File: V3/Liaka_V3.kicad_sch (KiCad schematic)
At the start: 0 parts

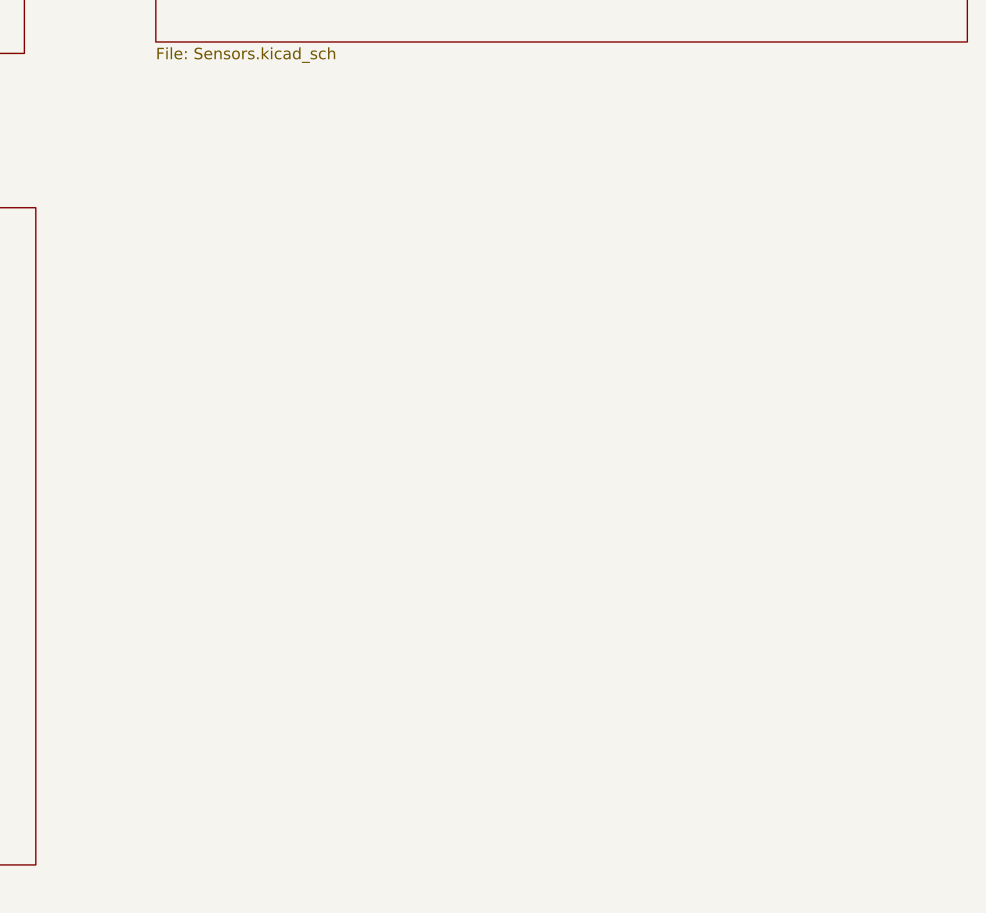
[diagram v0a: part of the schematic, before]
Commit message: Changed imu added flash chip
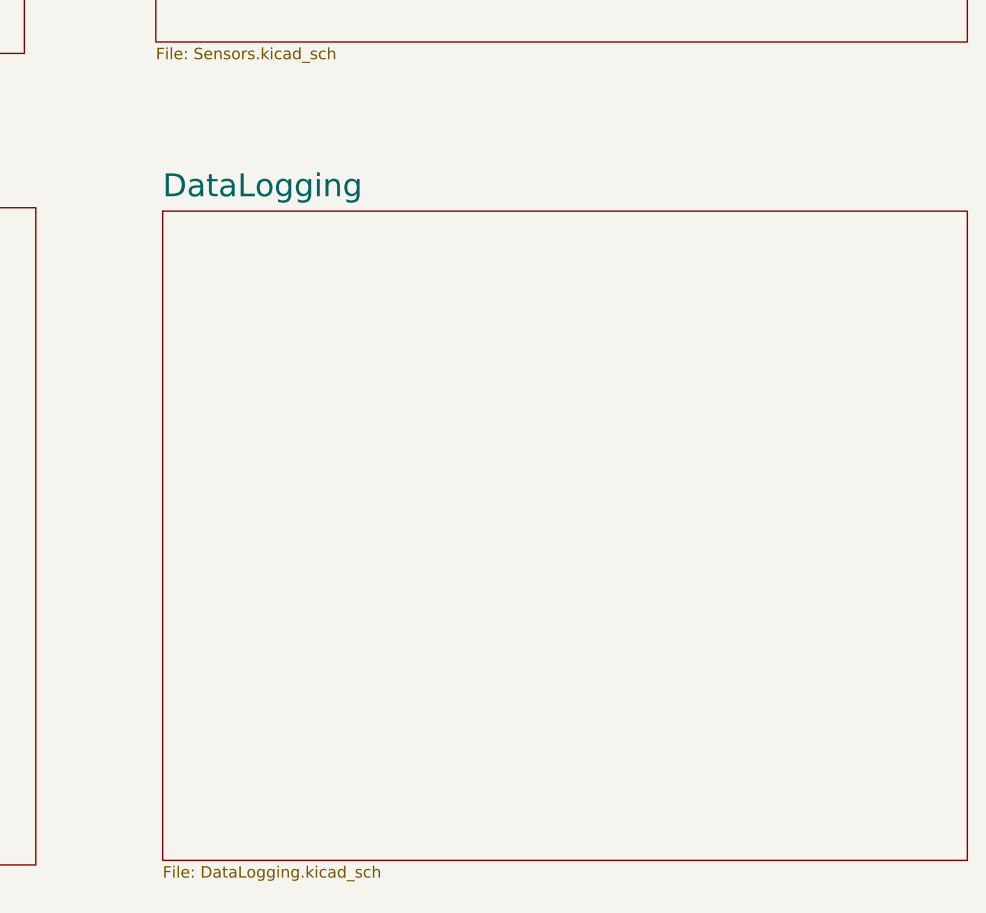
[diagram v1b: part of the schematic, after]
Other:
- added sheet DataLogging (DataLogging.kicad_sch)
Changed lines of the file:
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@@
+    )
+  )
+  (sheet (at 229.362 115.316) (size 89.408 72.136) (fields_autoplaced)
+    (stroke (width 0.1524) (type solid) (color 0 0 0 0))
+    (fill (color 8 253 255 0.2200))
+    (property "Sheet name" "DataLogging" (id 0) (at 229.362 113.9694 0)
+      (effects (font (size 2.54 2.54)) (justify left bottom))
+    )
+    (property "Sheet file" "DataLogging.kicad_sch" (id 1) (at 229.362 188.0366 0)
+      (effects (font (size 1.27 1.27)) (justify left top))
     )
   )
@@
     (path "/c1bf2b0b-bfb8-46f1-8af4-59d66c9f7f58" (page "5"))
     (path "/4e039e01-c7b4-4c31-a258-ecc90b9f543a" (page "6"))
+    (path "/38f95464-c4fd-44f7-9819-1304e1c28009" (page "7"))
   )
   (symbol_instances
@@
       (reference "#PWR?") (unit 1) (value "+BATT") (footprint "")
     )
-    (path "/4e039e01-c7b4-4c31-a258-ecc90b9f543a/07c49235-fb78-4b23-a52c-896dc2a9d0b2"
-      (reference "#PWR?") (unit 1) (value "VDD") (footprint "")
-    )
     (path "/c1bf2b0b-bfb8-46f1-8af4-59d66c9f7f58/0eab405b-23d8-4c86-88c9-b94c5ad9ac03"
       (reference "#PWR?") (unit 1) (value "VDD") (footprint "")
     )
+    (path "/38f95464-c4fd-44f7-9819-1304e1c28009/11e0f67b-3860-4d75-bf5e-a1dd240ae807"
+      (reference "#PWR?") (unit 1) (value "GND") (footprint "")
+    )
     (path "/eaec798d-40db-4341-9583-cf6858586b18/1334ff07-644a-4e89-a462-64abee627ba3"
       (reference "#PWR?") (unit 1) (value "GND") (footprint "")
@@
     (path "/c1bf2b0b-bfb8-46f1-8af4-59d66c9f7f58/1c8ba500-194e-4baa-9cad-123fef07ccc6"
       (reference "#PWR?") (unit 1) (value "GND") (footprint "")
-    )
-    (path "/035fef5e-61bd-47f2-9a8c-6b6e07e25123/1fe924ce-96e7-4bb6-a4d9-9df73dcec335"
-      (reference "#PWR?") (unit 1) (value "GND") (footprint "")
-    )
-    (path "/4e039e01-c7b4-4c31-a258-ecc90b9f543a/23abea24-afc9-432e-9d94-62254d9fbd31"
-      (reference "#PWR?") (unit 1) (value "GND") (footprint "")
-    )
-    (path "/035fef5e-61bd-47f2-9a8c-6b6e07e25123/276e171c-b034-4043-8c6a-12e4d29060fd"
-      (reference "#PWR?") (unit 1) (value "VDD") (footprint "")
     )
     (path "/c476245d-01b5-4ead-a36a-80ad0166f28f/2d4ff21e-1a71-4e64-948e-3321c7197cab"
@@
       (reference "#PWR?") (unit 1) (value "GND") (footprint "")
     )
-    (path "/035fef5e-61bd-47f2-9a8c-6b6e07e25123/56289dca-e8c2-4347-8f78-f6084529aac5"
-      (reference "#PWR?") (unit 1) (value "GND") (footprint "")
-    )
     (path "/eaec798d-40db-4341-9583-cf6858586b18/61f97263-beea-4b5f-8336-a396598572b6"
       (reference "#PWR?") (unit 1) (value "GND") (footprint "")
@@
       (reference "#PWR?") (unit 1) (value "GND") (footprint "")
     )
+    (path "/035fef5e-61bd-47f2-9a8c-6b6e07e25123/7484bfe0-5e4c-4d45-9bb0-21d86eb57d84"
+      (reference "#PWR?") (unit 1) (value "GND") (footprint "")
+    )
     (path "/4e039e01-c7b4-4c31-a258-ecc90b9f543a/76c2bd84-d071-44e5-9559-bbf53db59c32"
       (reference "#PWR?") (unit 1) (value "GND") (footprint "")
     )
-    (path "/035fef5e-61bd-47f2-9a8c-6b6e07e25123/77c6324b-d75c-41e6-b8c4-2dbbd6151dcc"
-      (reference "#PWR?") (unit 1) (value "GND") (footprint "")
-    )
     (path "/eaec798d-40db-4341-9583-cf6858586b18/7fdec674-5172-4407-842e-ac9dab14ff4b"
       (reference "#PWR?") (unit 1) (value "GND") (footprint "")
     )
-    (path "/035fef5e-61bd-47f2-9a8c-6b6e07e25123/89a88073-35ad-4134-994b-d2b633611865"
-      (reference "#PWR?") (unit 1) (value "GND") (footprint "")
-    )
     (path "/035fef5e-61bd-47f2-9a8c-6b6e07e25123/9167a978-4c05-4b30-a8e7-965c34dcd945"
       (reference "#PWR?") (unit 1) (value "GND") (footprint "")
@@
       (reference "#PWR?") (unit 1) (value "VDD") (footprint "")
     )
-    (path "/035fef5e-61bd-47f2-9a8c-6b6e07e25123/9aa644f9-f810-4651-870f-0b4511119721"
-      (reference "#PWR?") (unit 1) (value "VDD") (footprint "")
-    )
     (path "/4e039e01-c7b4-4c31-a258-ecc90b9f543a/9b089273-0232-4b74-abe7-187ee456ce87"
       (reference "#PWR?") (unit 1) (value "VDD") (footprint "")
@@
     )
     (path "/c1bf2b0b-bfb8-46f1-8af4-59d66c9f7f58/a757e2b6-3204-45b0-addf-84bbb6f14e24"
+      (reference "#PWR?") (unit 1) (value "VDD") (footprint "")
+    )
+    (path "/38f95464-c4fd-44f7-9819-1304e1c28009/ad871f17-203b-49ef-a572-a9044df3afba"
       (reference "#PWR?") (unit 1) (value "VDD") (footprint "")
     )
@@
       (reference "C?") (unit 1) (value "0.1uF") (footprint "Capacitor_SMD:C_0603_1608Metric")
     )
-    (path "/035fef5e-61bd-47f2-9a8c-6b6e07e25123/687ec28e-8447-4088-a25e-cad08d422e5b"
-      (reference "C?") (unit 1) (value "0.1uF") (footprint "Capacitor_SMD:C_0603_1608Metric")
-    )
     (path "/4e039e01-c7b4-4c31-a258-ecc90b9f543a/6b7f4f4e-3157-4279-9d13-af84c27a528c"
       (reference "C?") (unit 1) (value "100nF") (footprint "Capacitor_SMD:C_0603_1608Metric")
     )
-    (path "/035fef5e-61bd-47f2-9a8c-6b6e07e25123/7c20473d-bd4f-46be-bb5b-2605ef42748c"
-      (reference "C?") (unit 1) (value "0.1uF") (footprint "Capacitor_SMD:C_0603_1608Metric")
-    )
     (path "/c476245d-01b5-4ead-a36a-80ad0166f28f/84ce3cc7-ff73-468e-a5ac-44834b05bb62"
       (reference "C?") (unit 1) (value "100nF") (footprint "Capacitor_SMD:C_0603_1608Metric")
     )
-    (path "/035fef5e-61bd-47f2-9a8c-6b6e07e25123/862b6c52-73f7-4ca1-a0c2-9f7804e6291a"
-      (reference "C?") (unit 1) (value "10nF") (footprint "Capacitor_SMD:C_0603_1608Metric")
-    )
     (path "/035fef5e-61bd-47f2-9a8c-6b6e07e25123/91408aa9-edaa-48a7-a372-463a382e0fea"
       (reference "C?") (unit 1) (value "100nF") (footprint "Capacitor_SMD:C_0603_1608Metric")
@@
       (reference "C?") (unit 1) (value "1uF") (footprint "Capacitor_SMD:C_0603_1608Metric")
     )
-    (path "/035fef5e-61bd-47f2-9a8c-6b6e07e25123/fe42d64c-0a4e-4de8-8d3a-420b18659b04"
-      (reference "C?") (unit 1) (value "2.2nF") (footprint "Capacitor_SMD:C_0603_1608Metric")
-    )
     (path "/4e039e01-c7b4-4c31-a258-ecc90b9f543a/3872cb5b-a4e3-4e11-aa27-6615741d4736"
       (reference "D?") (unit 1) (value "LED_RED") (footprint "LED_SMD:LED_0603_1608Metric")
@@
       (reference "D?") (unit 1) (value "LED_BLUE") (footprint "LED_SMD:LED_0603_1608Metric")
     )
+    (path "/38f95464-c4fd-44f7-9819-1304e1c28009/35864471-14e5-48f0-aaee-c670f6735206"
+      (reference "J?") (unit 1) (value "THD2528-11SD-GF") (footprint "footprints:THD252811SDGF")
+    )
     (path "/c1bf2b0b-bfb8-46f1-8af4-59d66c9f7f58/36e751f5-18a2-4029-a838-454f4f91d302"
       (reference "J?") (unit 1) (value "SPI_Interface_Male") (footprint "Connector_PinHeader_2.54mm:PinHeader_1x04_P2.54mm_Vertical")
@@
       (reference "J?") (unit 1) (value "2-3S_LiPo_LARGE_HOLE_XT-30") (footprint "Connector_AMASS:AMASS_XT30PW-M_1x02_P2.50mm_Horizontal")
     )
-    (path "/4e039e01-c7b4-4c31-a258-ecc90b9f543a/d5c09f1d-d222-4bf2-aa6a-f7f07b671329"
-      (reference "J?") (unit 1) (value "THD2528-11SD-GF") (footprint "footprints:THD252811SDGF")
-    )
     (path "/c476245d-01b5-4ead-a36a-80ad0166f28f/faabba25-2e63-46b7-b7cc-3c89ba002db5"
       (reference "J?") (unit 1) (value "Conn_Coaxial") (footprint "Connector_Coaxial:SMA_Amphenol_132291_Vertical")
@@
       (reference "U?") (unit 1) (value "LM393") (footprint "Local_footprints:LM393DR2G")
     )
+    (path "/38f95464-c4fd-44f7-9819-1304e1c28009/470b8541-66d8-48de-a03d-e0da261b6c49"
+      (reference "U?") (unit 1) (value "M24M02-DRMN6TP") (footprint "SO_RMN6TP_STM")
+    )
     (path "/c476245d-01b5-4ead-a36a-80ad0166f28f/5a4f4295-d7bc-4d91-bcdf-8106d73d5c2f"
       (reference "U?") (unit 1) (value "RFM95W-915S2") (footprint "RF_Module:HOPERF_RFM9XW_SMD")
@@
       (reference "U?") (unit 1) (value "ESP32-WROOM-32") (footprint "RF_Module:ESP32-WROOM-32")
     )
-    (path "/035fef5e-61bd-47f2-9a8c-6b6e07e25123/b6663dc0-08da-497c-b183-19b0a0471464"
-      (reference "U?") (unit 1) (value "MPU-6050") (footprint "footprints:MPU-6050")
-    )
     (path "/c1bf2b0b-bfb8-46f1-8af4-59d66c9f7f58/c977a4d6-df26-4d85-bed7-f591bbf098cf"

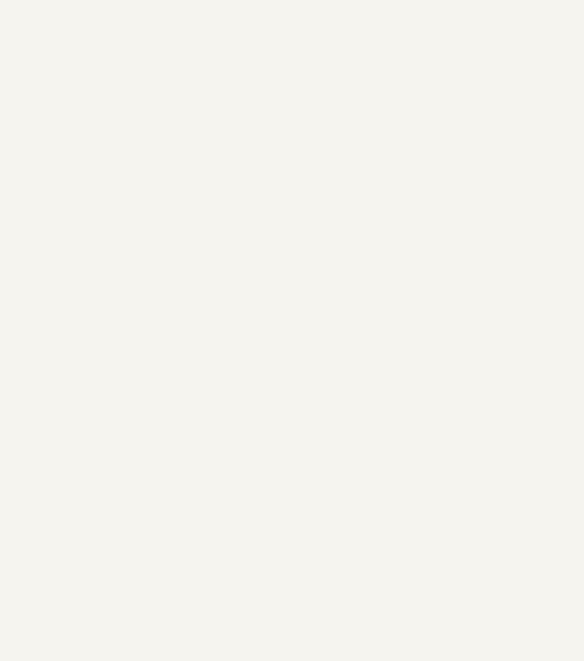
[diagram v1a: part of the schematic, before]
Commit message: Added sims, updated V3 board
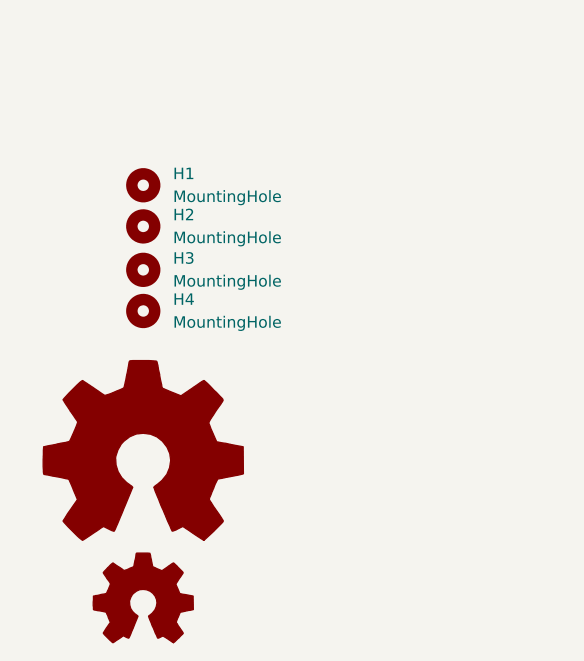
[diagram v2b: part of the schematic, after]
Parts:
- added H1, H2, H3, H4: MountingHole, MountingHole:MountingHole_3.2mm_M3_ISO14580_Pad_TopOnly, symbol Mechanical:MountingHole

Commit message: Updated costing sheet:
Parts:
- added H5: HPR_Logo, Local_footprints:HPR_Logo, symbol Mechanical:MountingHole
- added H6: Liaka_Text, Local_footprints:Liaka_Text, symbol Mechanical:MountingHole
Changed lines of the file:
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@@
-    )
-  )
-  (symbol (lib_id "Graphic:Logo_Open_Hardware_Large") (at 43.688 246.126 0) (unit 1)
-    (in_bom yes) (on_board yes) (fields_autoplaced)
-    (property "Reference" "#LOGO1" (id 0) (at 43.688 233.426 0)
-      (effects (font (size 1.27 1.27)) hide)
-    )
-    (property "Value" "Logo_Open_Hardware_Large" (id 1) (at 43.688 256.286 0)
-      (effects (font (size 1.27 1.27)) hide)
-    )
-    (property "Footprint" "Local_footprints:HPR_Logo" (id 2) (at 43.688 246.126 0)
-      (effects (font (size 1.27 1.27)) hide)
-    )
-    (property "Datasheet" "~" (id 3) (at 43.688 246.126 0)
-      (effects (font (size 1.27 1.27)) hide)
     )
   )
@@
     )
   )
-  (symbol (lib_id "Graphic:Logo_Open_Hardware_Small") (at 43.688 261.874 0) (unit 1)
+  (symbol (lib_id "Mechanical:MountingHole") (at 43.688 242.951 0) (unit 1)
     (in_bom yes) (on_board yes) (fields_autoplaced)
-    (property "Reference" "#LOGO2" (id 0) (at 43.688 254.889 0)
-      (effects (font (size 1.27 1.27)) hide)
-    )
-    (property "Value" "Logo_Open_Hardware_Small" (id 1) (at 43.688 267.589 0)
-      (effects (font (size 1.27 1.27)) hide)
-    )
-    (property "Footprint" "Local_footprints:Liaka_Text" (id 2) (at 43.688 261.874 0)
-      (effects (font (size 1.27 1.27)) hide)
-    )
-    (property "Datasheet" "~" (id 3) (at 43.688 261.874 0)
+    (property "Reference" "H5" (id 0) (at 46.99 241.6809 0)
+      (effects (font (size 1.27 1.27)) (justify left))
+    )
+    (property "Value" "HPR_Logo" (id 1) (at 46.99 244.2209 0)
+      (effects (font (size 1.27 1.27)) (justify left))
+    )
+    (property "Footprint" "Local_footprints:HPR_Logo" (id 2) (at 43.688 242.951 0)
+      (effects (font (size 1.27 1.27)) hide)
+    )
+    (property "Datasheet" "~" (id 3) (at 43.688 242.951 0)
+      (effects (font (size 1.27 1.27)) hide)
+    )
+  )
+  (symbol (lib_id "Mechanical:MountingHole") (at 43.688 248.412 0) (unit 1)
+    (in_bom yes) (on_board yes) (fields_autoplaced)
+    (property "Reference" "H6" (id 0) (at 46.99 247.1419 0)
+      (effects (font (size 1.27 1.27)) (justify left))
+    )
+    (property "Value" "Liaka_Text" (id 1) (at 46.99 249.6819 0)
+      (effects (font (size 1.27 1.27)) (justify left))
+    )
+    (property "Footprint" "Local_footprints:Liaka_Text" (id 2) (at 43.688 248.412 0)
+      (effects (font (size 1.27 1.27)) hide)
+    )
+    (property "Datasheet" "~" (id 3) (at 43.688 248.412 0)
       (effects (font (size 1.27 1.27)) hide)
     )
@@
   )
   (symbol_instances
-    (path "/54a084a5-cb7c-429e-a9b1-bab5f7a63bfd"
-      (reference "#LOGO1") (unit 1) (value "Logo_Open_Hardware_Large") (footprint "Local_footprints:HPR_Logo")
-    )
-    (path "/c6735cec-50af-424d-99bb-8bb67387d9c3"
-      (reference "#LOGO2") (unit 1) (value "Logo_Open_Hardware_Small") (footprint "Local_footprints:Liaka_Text")
-    )
     (path "/035fef5e-61bd-47f2-9a8c-6b6e07e25123/7484bfe0-5e4c-4d45-9bb0-21d86eb57d84"
       (reference "#PWR0101") (unit 1) (value "GND") (footprint "")
@@
       (reference "#PWR0141") (unit 1) (value "VDD") (footprint "")
     )
-    (path "/c1bf2b0b-bfb8-46f1-8af4-59d66c9f7f58/516b1998-f83d-4554-8bcc-ec96986a9cc9"
-      (reference "#PWR0142") (unit 1) (value "VDC") (footprint "")
+    (path "/035fef5e-61bd-47f2-9a8c-6b6e07e25123/05a33a53-3485-40ff-a402-f4e8d0f8d1f2"
+      (reference "#PWR0142") (unit 1) (value "GND") (footprint "")
     )
     (path "/c1bf2b0b-bfb8-46f1-8af4-59d66c9f7f58/a757e2b6-3204-45b0-addf-84bbb6f14e24"
@@
       (reference "H4") (unit 1) (value "MountingHole") (footprint "MountingHole:MountingHole_3.2mm_M3_ISO14580_Pad_TopOnly")
     )
+    (path "/7aacbe2c-6632-4bd7-82d1-77578561c593"
+      (reference "H5") (unit 1) (value "HPR_Logo") (footprint "Local_footprints:HPR_Logo")
+    )
+    (path "/b662713a-c52f-4d24-bac4-0376034f0a96"
+      (reference "H6") (unit 1) (value "Liaka_Text") (footprint "Local_footprints:Liaka_Text")
+    )
     (path "/38f95464-c4fd-44f7-9819-1304e1c28009/a5312ff8-76b4-4cdf-8d2f-5b53f0e4b8a6"
       (reference "IC1") (unit 1) (value "XTSD04GLGEAG") (footprint "SON127P800X600X95-8N")
@@
     )
     (path "/eaec798d-40db-4341-9583-cf6858586b18/38830973-56f5-44f0-82cb-ac0944a4658c"
-      (reference "R2") (unit 1) (value "50k") (footprint "Resistor_SMD:R_0603_1608Metric")
+      (reference "R2") (unit 1) (value "56k") (footprint "Resistor_SMD:R_0603_1608Metric")
     )
     (path "/eaec798d-40db-4341-9583-cf6858586b18/640eccb5-8f7b-4e0e-ae8d-1c1155f84f6f"
